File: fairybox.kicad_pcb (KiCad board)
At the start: 2 copper layers, 91.4 x 55.9 mm, 65 parts, among them J1 REED, Q1 locked, Q10 locked, Q2 locked, Q3 locked, Q4 locked, Q5 locked, Q6 locked, Q7 locked, Q8 locked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

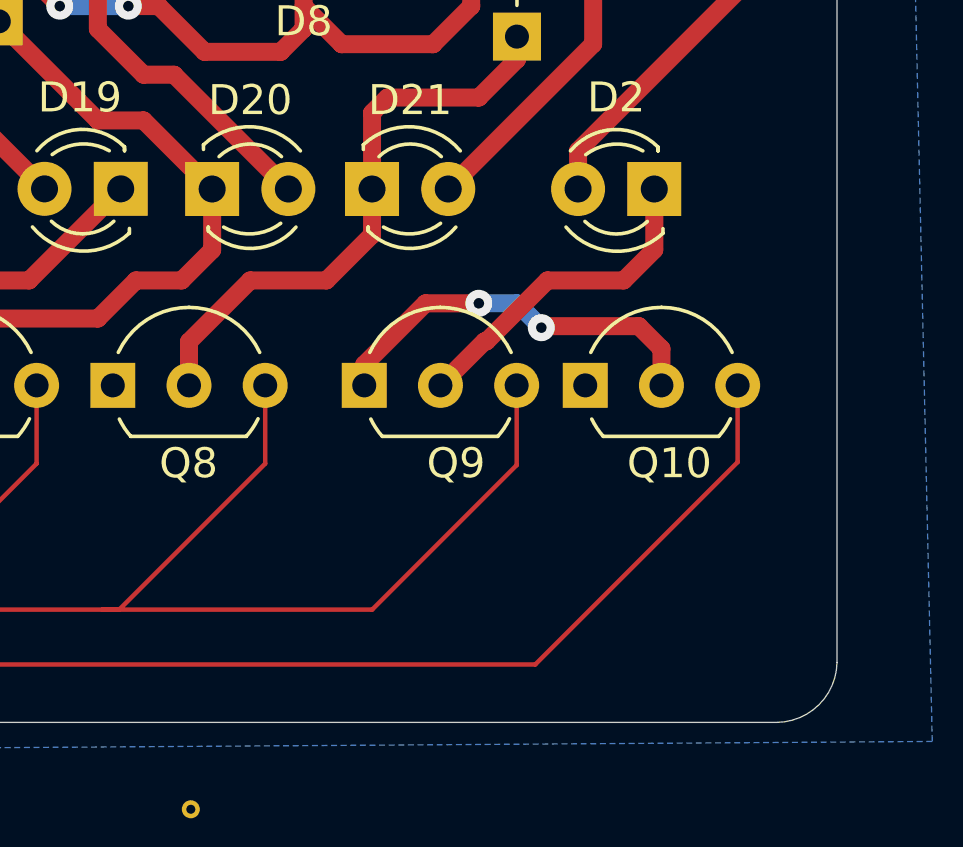
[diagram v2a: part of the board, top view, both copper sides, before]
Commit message: Eliminating Q10_COL via
Re-routed Q9_COL around Q9 to eliminate the need for the Q10_COL net via.
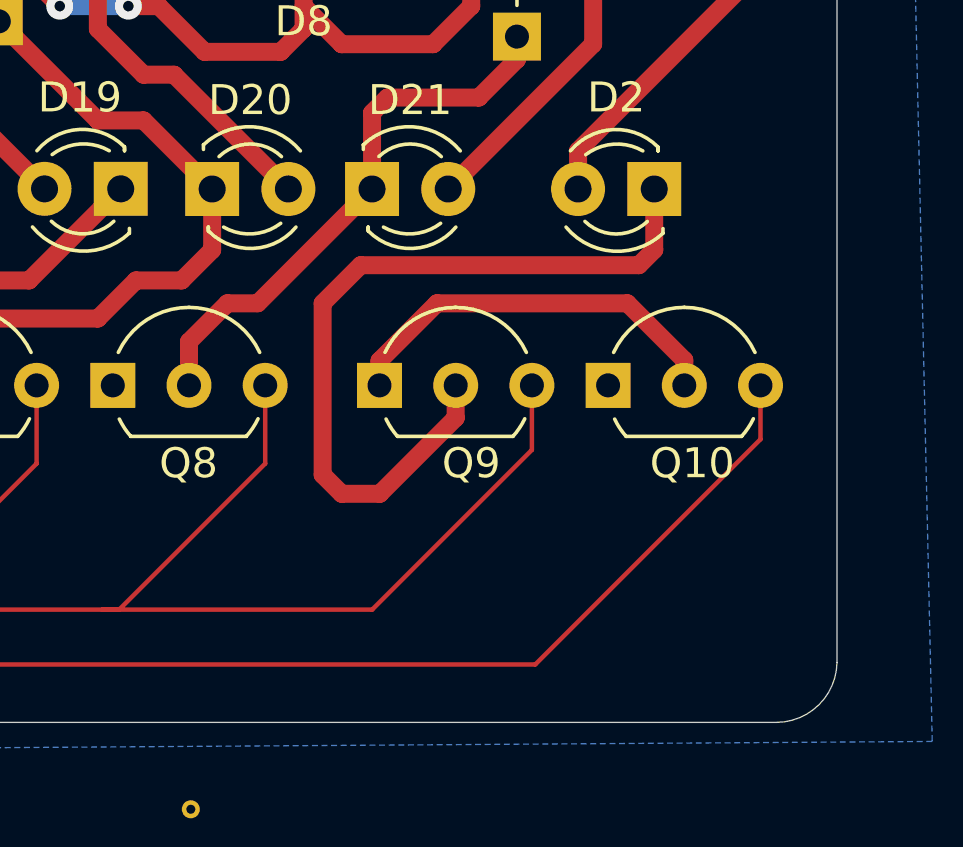
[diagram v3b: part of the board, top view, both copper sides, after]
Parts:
- moved Q10 0.76 mm to (134.6, 95.4)
- moved Q9 0.51 mm to (127.0, 95.4)
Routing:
- net /Q9_COL: track 11.0 -> 26.4 mm
- net /Q8_COL: track 19.2 -> 18.3 mm
- net /Q10_COL: track 13.3 -> 13.4 mm, vias 2 -> 0
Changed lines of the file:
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@@
     )
   )
-  (footprint "Package_TO_SOT_THT:TO-92L_Inline_Wide" locked (layer "F.Cu")
-    (at 133.848 95.446)
+  (footprint "Package_TO_SOT_THT:TO-92L_Inline_Wide" (layer "F.Cu")
+    (at 134.61 95.446)
     (descr "TO-92L leads in-line (large body variant of TO-92), also known as TO-226, wide, drill 0.75mm (see https://www.diodes.com/assets/Package-Files/TO92L.pdf and http://www.ti.com/lit/an/snoa059/snoa059.pdf)")
     (tags "TO-92L Inline Wide transistor")
@@
   )
   (footprint "Package_TO_SOT_THT:TO-92L_Inline_Wide" (layer "F.Cu")
-    (at 126.482 95.446)
+    (at 126.99 95.446)
     (descr "TO-92L leads in-line (large body variant of TO-92), also known as TO-226, wide, drill 0.75mm (see https://www.diodes.com/assets/Package-Files/TO92L.pdf and http://www.ti.com/lit/an/snoa059/snoa059.pdf)")
     (tags "TO-92L Inline Wide transistor")
@@
   (via (at 116.332 82.804) (size 0.9) (drill 0.35) (layers "F.Cu" "B.Cu") (net 5))
   (segment (start 116.332 82.804) (end 118.618 82.804) (width 0.6) (layer "B.Cu") (net 5))
-  (segment (start 135.128 91.948) (end 136.149 90.927) (width 0.6) (layer "F.Cu") (net 6))
-  (segment (start 129.022 95.446) (end 130.488 93.98) (width 0.6) (layer "F.Cu") (net 6))
-  (segment (start 130.556 93.98) (end 132.588 91.948) (width 0.6) (layer "F.Cu") (net 6))
-  (segment (start 136.149 90.927) (end 136.149 88.9) (width 0.6) (layer "F.Cu") (net 6))
-  (segment (start 132.588 91.948) (end 135.128 91.948) (width 0.6) (layer "F.Cu") (net 6))
-  (segment (start 130.488 93.98) (end 130.556 93.98) (width 0.6) (layer "F.Cu") (net 6))
+  (segment (start 127 99.06) (end 129.53 96.53) (width 0.6) (layer "F.Cu") (net 6))
+  (segment (start 125.73 99.06) (end 127 99.06) (width 0.6) (layer "F.Cu") (net 6))
+  (segment (start 136.149 88.9) (end 136.149 90.927) (width 0.6) (layer "F.Cu") (net 6))
+  (segment (start 129.53 96.53) (end 129.53 95.446) (width 0.6) (layer "F.Cu") (net 6))
+  (segment (start 135.636 91.44) (end 126.365 91.44) (width 0.6) (layer "F.Cu") (net 6))
+  (segment (start 126.365 91.44) (end 125.095 92.71) (width 0.6) (layer "F.Cu") (net 6))
+  (segment (start 125.095 98.425) (end 125.73 99.06) (width 0.6) (layer "F.Cu") (net 6))
+  (segment (start 136.149 90.927) (end 135.636 91.44) (width 0.6) (layer "F.Cu") (net 6))
+  (segment (start 125.095 92.71) (end 125.095 98.425) (width 0.6) (layer "F.Cu") (net 6))
   (segment (start 105.6386 92.075) (end 108.204 89.5096) (width 0.15) (layer "F.Cu") (net 7))
   (segment (start 107.95 98.0948) (end 107.0864 98.9584) (width 0.15) (layer "F.Cu") (net 7))
@@
   (segment (start 89.7766 83.2234) (end 92.456 85.9028) (width 0.15) (layer "F.Cu") (net 8))
   (segment (start 88.5 83.25) (end 87.63 82.38) (width 0.15) (layer "F.Cu") (net 8))
+  (segment (start 69.215 106.045) (end 67.945 104.775) (width 0.15) (layer "F.Cu") (net 9))
   (segment (start 100.4316 104.7496) (end 132.1816 104.7496) (width 0.15) (layer "F.Cu") (net 9))
-  (segment (start 69.215 106.045) (end 67.945 104.775) (width 0.15) (layer "F.Cu") (net 9))
   (segment (start 98.3107 102.6795) (end 98.7552 102.235) (width 0.15) (layer "F.Cu") (net 9))
+  (segment (start 132.1816 104.7496) (end 139.69 97.2412) (width 0.15) (layer "F.Cu") (net 9))
   (segment (start 64.135 105.537) (end 64.643 106.045) (width 0.15) (layer "F.Cu") (net 9))
   (segment (start 76.19 102.86) (end 76.19 95.065) (width 0.15) (layer "F.Cu") (net 9))
+  (segment (start 98.9076 103.2256) (end 100.4316 104.7496) (width 0.15) (layer "F.Cu") (net 9))
   (segment (start 64.643 106.045) (end 94.9452 106.045) (width 0.15) (layer "F.Cu") (net 9))
-  (segment (start 138.928 98.0032) (end 138.928 95.446) (width 0.15) (layer "F.Cu") (net 9))
   (segment (start 67.945 104.775) (end 66.675 104.775) (width 0.15) (layer "F.Cu") (net 9))
-  (segment (start 98.9076 103.2256) (end 100.4316 104.7496) (width 0.15) (layer "F.Cu") (net 9))
   (segment (start 79.375 106.045) (end 76.19 102.86) (width 0.15) (layer "F.Cu") (net 9))
+  (segment (start 139.69 97.2412) (end 139.69 95.446) (width 0.15) (layer "F.Cu") (net 9))
   (segment (start 98.3107 102.6541) (end 98.9076 102.0572) (width 0.15) (layer "F.Cu") (net 9))
+  (segment (start 98.9076 102.0572) (end 98.9076 103.2256) (width 0.15) (layer "F.Cu") (net 9))
   (segment (start 99.695 90.7034) (end 98.9076 91.4908) (width 0.15) (layer "F.Cu") (net 9))
   (segment (start 64.135 104.775) (end 64.135 105.537) (width 0.15) (layer "F.Cu") (net 9))
   (segment (start 94.9452 106.045) (end 98.3107 102.6795) (width 0.15) (layer "F.Cu") (net 9))
-  (segment (start 98.9076 102.0572) (end 98.9076 103.2256) (width 0.15) (layer "F.Cu") (net 9))
   (segment (start 98.3107 102.6795) (end 98.3107 102.6541) (width 0.15) (layer "F.Cu") (net 9))
-  (segment (start 132.1816 104.7496) (end 138.928 98.0032) (width 0.15) (layer "F.Cu") (net 9))
   (segment (start 98.9076 91.4908) (end 98.9076 102.0572) (width 0.15) (layer "F.Cu") (net 9))
   (segment (start 99.695 89.154) (end 99.695 90.7034) (width 0.15) (layer "F.Cu") (net 9))
@@
   (segment (start 129.281 88.9) (end 134.112 84.069) (width 0.6) (layer "F.Cu") (net 24))
   (segment (start 131.572 84.582) (end 130.302 85.852) (width 0.6) (layer "F.Cu") (net 25))
-  (segment (start 126.741 90.429) (end 126.741 88.9) (width 0.6) (layer "F.Cu") (net 25))
+  (segment (start 120.64 95.25) (end 120.64 93.99) (width 0.6) (layer "F.Cu") (net 25))
   (segment (start 131.572 83.82) (end 131.572 84.582) (width 0.6) (layer "F.Cu") (net 25))
   (segment (start 126.741 86.365) (end 126.741 88.9) (width 0.6) (layer "F.Cu") (net 25))
   (segment (start 127.254 85.852) (end 126.741 86.365) (width 0.6) (layer "F.Cu") (net 25))
-  (segment (start 120.64 95.25) (end 120.64 93.99) (width 0.6) (layer "F.Cu") (net 25))
+  (segment (start 122.931 92.71) (end 126.741 88.9) (width 0.6) (layer "F.Cu") (net 25))
   (segment (start 130.302 85.852) (end 127.254 85.852) (width 0.6) (layer "F.Cu") (net 25))
-  (segment (start 125.222 91.948) (end 126.741 90.429) (width 0.6) (layer "F.Cu") (net 25))
-  (segment (start 122.682 91.948) (end 125.222 91.948) (width 0.6) (layer "F.Cu") (net 25))
-  (segment (start 120.64 93.99) (end 122.682 91.948) (width 0.6) (layer "F.Cu") (net 25))
+  (segment (start 120.64 93.99) (end 121.92 92.71) (width 0.6) (layer "F.Cu") (net 25))
+  (segment (start 121.92 92.71) (end 122.931 92.71) (width 0.6) (layer "F.Cu") (net 25))
   (segment (start 65.9384 97.8916) (end 68.1736 97.8916) (width 0.6) (layer "F.Cu") (net 26))
   (segment (start 64.135 99.695) (end 65.9384 97.8916) (width 0.6) (layer "F.Cu") (net 26))
@@
   (segment (start 115.824 88.895) (end 110.49 83.561) (width 0.6) (layer "F.Cu") (net 31))
   (segment (start 110.49 83.561) (end 110.49 81.18) (width 0.6) (layer "F.Cu") (net 31))
-  (segment (start 128.524 92.71) (end 126.482 94.752) (width 0.6) (layer "F.Cu") (net 32))
-  (segment (start 132.435082 93.472) (end 135.636 93.472) (width 0.6) (layer "F.Cu") (net 32))
-  (segment (start 132.384541 93.522541) (end 132.435082 93.472) (width 0.6) (layer "F.Cu") (net 32))
-  (segment (start 126.482 94.752) (end 126.482 95.446) (width 0.6) (layer "F.Cu") (net 32))
-  (segment (start 130.302 92.71) (end 128.524 92.71) (width 0.6) (layer "F.Cu") (net 32))
-  (segment (start 135.636 93.472) (end 136.388 94.224) (width 0.6) (layer "F.Cu") (net 32))
-  (segment (start 136.388 94.224) (end 136.388 95.446) (width 0.6) (layer "F.Cu") (net 32))
-  (via (at 130.302 92.71) (size 0.9) (drill 0.35) (layers "F.Cu" "B.Cu") (net 32))
-  (via (at 132.384541 93.522541) (size 0.9) (drill 0.35) (layers "F.Cu" "B.Cu") (net 32))
-  (segment (start 131.572 92.71) (end 132.384541 93.522541) (width 0.6) (layer "B.Cu") (net 32))
-  (segment (start 130.302 92.71) (end 131.572 92.71) (width 0.6) (layer "B.Cu") (net 32))
+  (segment (start 128.905 92.71) (end 135.255 92.71) (width 0.6) (layer "F.Cu") (net 32))
+  (segment (start 126.99 95.446) (end 126.99 94.625) (width 0.6) (layer "F.Cu") (net 32))
+  (segment (start 137.15 94.605) (end 137.15 95.446) (width 0.6) (layer "F.Cu") (net 32))
+  (segment (start 135.255 92.71) (end 137.15 94.605) (width 0.6) (layer "F.Cu") (net 32))
+  (segment (start 126.99 94.625) (end 128.905 92.71) (width 0.6) (layer "F.Cu") (net 32))
   (segment (start 87.376 85.09) (end 84.582 82.296) (width 0.6) (layer "F.Cu") (net 33))
   (segment (start 84.582 82.296) (end 84.582 81.28) (width 0.6) (layer "F.Cu") (net 33))
@@
   (segment (start 54.864 75.692) (end 56.896 73.66) (width 0.2) (layer "B.Cu") (net 37))
   (segment (start 96.52 76.2) (end 96.52 78.359) (width 0.15) (layer "F.Cu") (net 39))
+  (segment (start 132.07 97.5968) (end 126.746 102.9208) (width 0.15) (layer "F.Cu") (net 39))
   (segment (start 97.155 84.8614) (end 97.155 78.994) (width 0.15) (layer "F.Cu") (net 39))
   (segment (start 104.3432 87.3252) (end 102.87 85.852) (width 0.15) (layer "F.Cu") (net 39))
@@
   (segment (start 104.3432 89.7128) (end 104.3432 87.3252) (width 0.15) (layer "F.Cu") (net 39))
   (segment (start 103.124 90.932) (end 104.3432 89.7128) (width 0.15) (layer "F.Cu") (net 39))
-  (segment (start 131.562 98.1048) (end 126.746 102.9208) (width 0.15) (layer "F.Cu") (net 39))
   (segment (start 117.7544 102.9208) (end 101.4476 102.9208) (width 0.15) (layer "F.Cu") (net 39))
   (segment (start 98.1456 85.852) (end 97.155 84.8614) (width 0.15) (layer "F.Cu") (net 39))
   (segment (start 101.4476 102.9208) (end 99.6188 101.092) (width 0.15) (layer "F.Cu") (net 39))
-  (segment (start 131.562 95.446) (end 131.562 98.1048) (width 0.15) (layer "F.Cu") (net 39))
+  (segment (start 132.07 95.446) (end 132.07 97.5968) (width 0.15) (layer "F.Cu") (net 39))
   (segment (start 99.6188 101.092) (end 99.6188 92.4052) (width 0.15) (layer "F.Cu") (net 39))
   (segment (start 118.3132 102.9208) (end 117.7544 102.9208) (width 0.15) (layer "F.Cu") (net 39))

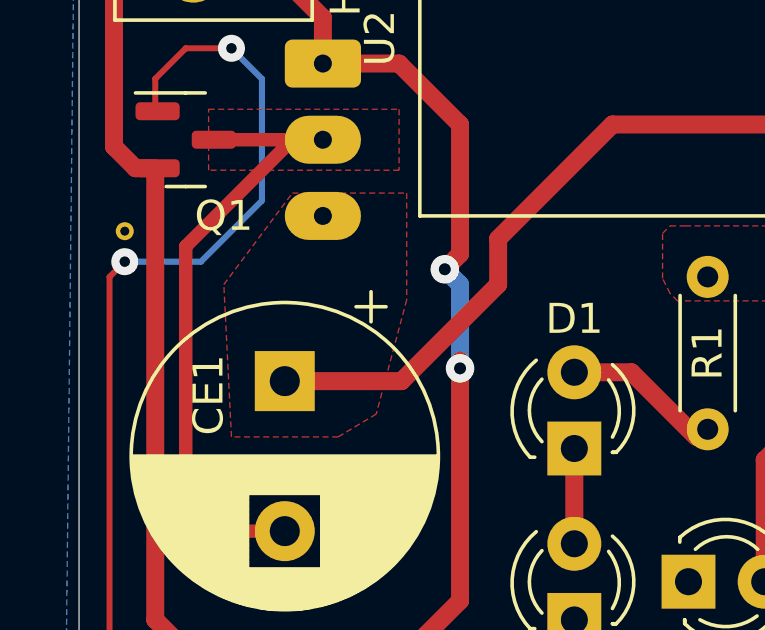
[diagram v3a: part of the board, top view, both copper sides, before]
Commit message: Removed bulk capacitor power puddle
Replaced CE1<>U2 copper pour with a 0.600mm track.
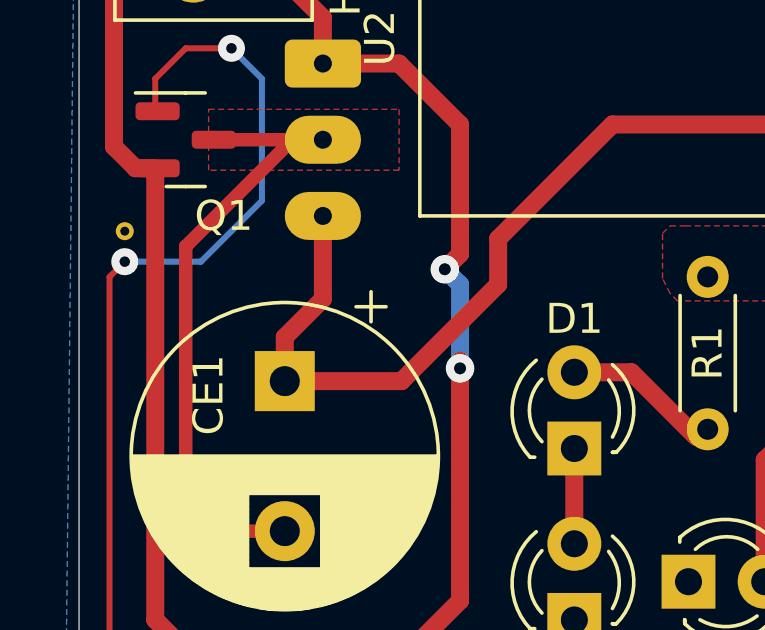
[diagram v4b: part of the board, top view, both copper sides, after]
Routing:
- net +5V: track 100.8 -> 106.8 mm
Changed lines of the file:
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@@
   (segment (start 58.42 93.472) (end 58.42 94.996) (width 0.2) (layer "F.Cu") (net 12))
   (segment (start 58.42 94.996) (end 57.531 95.885) (width 0.2) (layer "F.Cu") (net 12))
+  (segment (start 57.658 78.2066) (end 58.928 76.9366) (width 0.6) (layer "F.Cu") (net 13))
   (segment (start 111.76 73.914) (end 110.49 75.184) (width 0.6) (layer "F.Cu") (net 13))
   (segment (start 61.549677 79.674323) (end 57.658 79.674323) (width 0.6) (layer "F.Cu") (net 13))
   (segment (start 128.516 74.668) (end 128.516 76.2) (width 0.6) (layer "F.Cu") (net 13))
   (segment (start 107.696 74.422) (end 108.204 74.422) (width 0.6) (layer "F.Cu") (net 13))
+  (segment (start 58.928 76.9366) (end 58.928 74.168) (width 0.6) (layer "F.Cu") (net 13))
   (segment (start 64.77 76.454) (end 64.77 74.93) (width 0.6) (layer "F.Cu") (net 13))
   (segment (start 64.77 74.93) (end 68.58 71.12) (width 0.6) (layer "F.Cu") (net 13))
+  (segment (start 57.658 79.674323) (end 57.658 78.2066) (width 0.6) (layer "F.Cu") (net 13))
   (segment (start 94.615 78.994) (end 91.46 78.994) (width 0.6) (layer "F.Cu") (net 13))
   (segment (start 104.394 71.12) (end 107.696 74.422) (width 0.6) (layer "F.Cu") (net 13))
@@
       )
     )
-  )
-  (zone (net 13) (net_name "+5V") (layer "F.Cu") (name "1") (hatch edge 0.508)
-    (priority 1)
-    (connect_pads (clearance 0))
-    (min_thickness 0.254) (filled_areas_thickness no)
-    (fill yes (thermal_gap 0.508) (thermal_bridge_width 0.508) (smoothing fillet))
-    (polygon
-      (pts
-        (xy 61.722 76.962)
-        (xy 60.706 80.772)
-        (xy 59.436 81.534)
-        (xy 58.42 81.534)
-        (xy 55.88 81.534)
-        (xy 55.626 76.454)
-        (xy 57.912 73.406)
-        (xy 61.722 73.406)
-      )
-    )
